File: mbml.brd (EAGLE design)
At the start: 74.9 x 72.4 mm, 44 parts, among them K1 G5SB, K2 68800611622, Q1 2N2222, Q2 IRLZ24LPBF, U1 REG_5V_SWITCHING_SI-8050E, X1 43160-1102, X2 CON-2

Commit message: Set correct values for button LED current limiting resistors
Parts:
- R10: value 470 -> 10k
- R9: value 1.8k -> 3.3k
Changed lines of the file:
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@@
 <attribute name="NAME" x="52.832" y="53.086" size="0.6096" layer="25"/>
 </element>
-<element name="R9" library="resistor" package="0204/5" value="1.8k" x="41.91" y="25.4" smashed="yes" rot="R270">
+<element name="R9" library="resistor" package="0204/5" value="3.3k" x="41.91" y="25.4" smashed="yes" rot="R270">
 <attribute name="NAME" x="42.2656" y="29.2354" size="0.9906" layer="25" ratio="10" rot="R90"/>
 <attribute name="VALUE" x="39.5986" y="27.5336" size="0.9906" layer="27" ratio="10" rot="R270"/>
 </element>
-<element name="R10" library="resistor" package="0204/5" value="470" x="45.72" y="25.4" smashed="yes" rot="R270">
+<element name="R10" library="resistor" package="0204/5" value="10k" x="45.72" y="25.4" smashed="yes" rot="R270">
 <attribute name="NAME" x="46.0756" y="29.2354" size="0.9906" layer="25" ratio="10" rot="R90"/>
 <attribute name="VALUE" x="43.4086" y="27.5336" size="0.9906" layer="27" ratio="10" rot="R270"/>

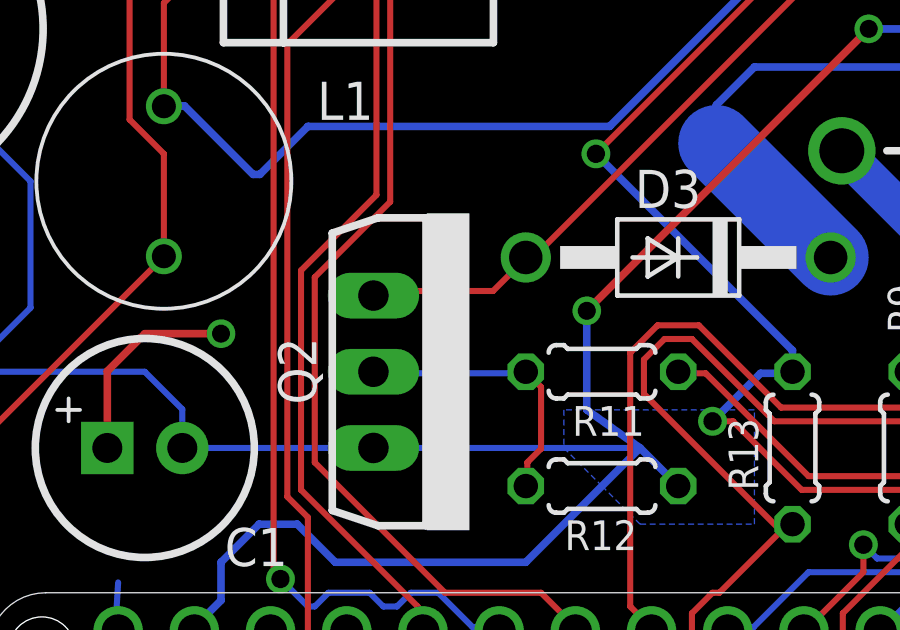
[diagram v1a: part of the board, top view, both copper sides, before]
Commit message: MBMLV2.2
Fixed backwards pins on fan MOSFET, added note about switching 5V
regulator to a version that supports a higher current draw.
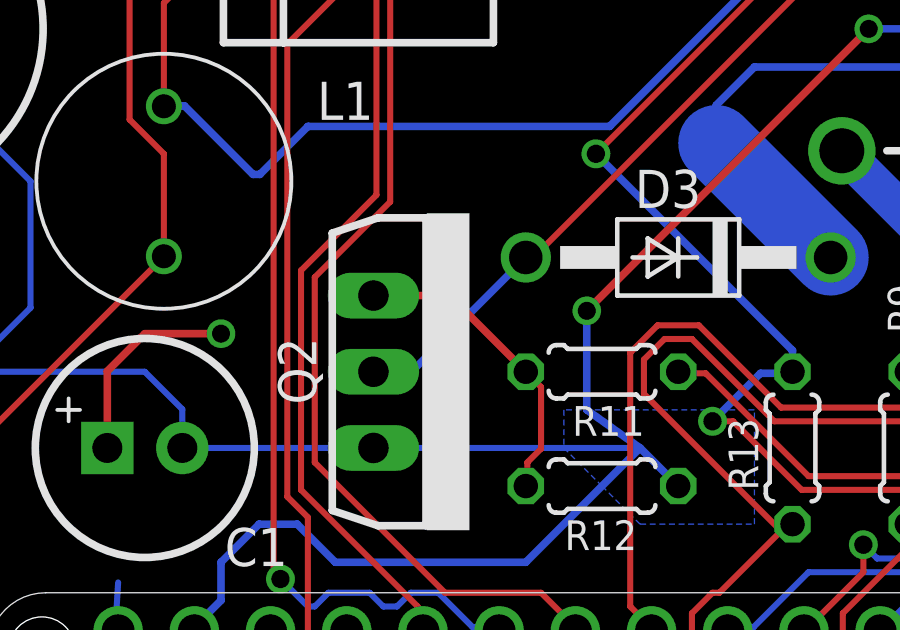
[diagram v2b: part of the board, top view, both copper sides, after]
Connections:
- net N$10: now also Q2.1; no longer Q2.2
- net N$9: now also Q2.2; no longer Q2.1
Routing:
- net N$10: track 9.32 -> 10.4 mm
- net N$9: track 58.8 -> 59.8 mm
